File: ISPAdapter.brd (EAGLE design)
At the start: 68 x 38 mm, 4 parts

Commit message: Tweaks
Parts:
- moved JP2 0.92 mm to (33.4, 36.0)
- moved JP1 0.70 mm to (41.0, 36.0)
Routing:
- net GND: track 1.41 -> 2.40 mm
- net VCC: track 52.9 -> 52.1 mm
- net DGND: track 44.4 -> 43.6 mm
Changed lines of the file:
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@@
 <hole x="57" y="21" drill="2"/>
 <hole x="15" y="21" drill="2"/>
-<text x="41.7" y="34" size="1" layer="107" font="vector" ratio="20" rot="SR270" align="center-left">GND</text>
-<text x="44.3" y="34" size="1" layer="107" font="vector" ratio="20" rot="SR270" align="center-left">+5V</text>
+<text x="41" y="34" size="1" layer="107" font="vector" ratio="20" rot="SR270" align="center-left">GND</text>
+<text x="43.6" y="34" size="1" layer="107" font="vector" ratio="20" rot="SR270" align="center-left">+5V</text>
 <text x="26" y="11" size="1" layer="107" font="vector" ratio="20" rot="SR0">1 MISO</text>
 <text x="19" y="11" size="1" layer="107" font="vector" ratio="20" rot="SR0">2 VCC</text>
@@
 <wire x1="18" y1="10" x2="18" y2="17" width="0.2032" layer="107"/>
 <wire x1="25" y1="17" x2="25" y2="10" width="0.2032" layer="107"/>
-<text x="22.6" y="23.5" size="0.8128" layer="107" font="vector" ratio="20" align="top-center">1</text>
-<text x="21.6" y="23.5" size="0.8128" layer="107" font="vector" ratio="20" align="top-center">2</text>
-<text x="20.6" y="23.5" size="0.8128" layer="107" font="vector" ratio="20" align="top-center">3</text>
-<text x="19.6" y="23.5" size="0.8128" layer="107" font="vector" ratio="20" align="top-center">4</text>
-<text x="18.6" y="23.5" size="0.8128" layer="107" font="vector" ratio="20" align="top-center">5</text>
-<text x="17.6" y="23.5" size="0.8128" layer="107" font="vector" ratio="20" align="top-center">6</text>
+<text x="22.6" y="23.4" size="0.8128" layer="107" font="vector" ratio="20" align="top-center">1</text>
+<text x="21.6" y="23.4" size="0.8128" layer="107" font="vector" ratio="20" align="top-center">2</text>
+<text x="20.6" y="23.4" size="0.8128" layer="107" font="vector" ratio="20" align="top-center">3</text>
+<text x="19.6" y="23.4" size="0.8128" layer="107" font="vector" ratio="20" align="top-center">4</text>
+<text x="18.6" y="23.4" size="0.8128" layer="107" font="vector" ratio="20" align="top-center">5</text>
+<text x="17.6" y="23.4" size="0.8128" layer="107" font="vector" ratio="20" align="top-center">6</text>
 <circle x="27" y="30.4" radius="1.7" width="0.5" layer="107"/>
 <hole x="36" y="11.6" drill="2"/>
@@
 <circle x="36" y="6.9" radius="1.7" width="0.5" layer="107"/>
 <circle x="15" y="21" radius="1.7" width="0.5" layer="107"/>
-<text x="34.3" y="34" size="1" layer="107" font="vector" ratio="20" rot="SR270" align="center-left">GND</text>
+<text x="33.4" y="34" size="1" layer="107" font="vector" ratio="20" rot="SR270" align="center-left">GND</text>
 </plain>
 <attributes>
@@
 <param name="srMinRoundness" value="0mil"/>
 <param name="srMaxRoundness" value="0mil"/>
-<param name="slThermalIsolate" value="10mil"/>
+<param name="slThermalIsolate" value="20mil"/>
 <param name="slThermalsForVias" value="0"/>
 <param name="dpMaxLengthDifference" value="10mm"/>
@@
 <attribute name="DIGIKEY_PART_#" value="732-5394-ND" x="6" y="19" size="1.778" layer="27" display="off"/>
 </element>
-<element name="JP1" library="SparkFun-Connectors" package="1X02" value="M02PTH" x="41.7" y="36"/>
+<element name="JP1" library="SparkFun-Connectors" package="1X02" value="M02PTH" x="41" y="36"/>
 <element name="U$1" library="dubec" package="AVX9258-8P" value="AVX9258" x="19" y="27">
 <attribute name="MANUFACTURER" value="AVX Corporation" x="19" y="27" size="1.778" layer="27" display="off"/>
@@
 <attribute name="DIGIKEY_PART_#" value="478-5495-1-ND" x="19" y="27" size="1.778" layer="27" display="off"/>
 </element>
-<element name="JP2" library="SparkFun-Connectors" package="1X01" value="M01PTH" x="34.3" y="36"/>
+<element name="JP2" library="SparkFun-Connectors" package="1X01" value="M01PTH" x="33.38" y="36"/>
 </elements>
 <signals>
@@
 <contactref element="JP1" pad="2"/>
 <contactref element="U$1" pad="2"/>
-<wire x1="44.24" y1="36" x2="35.66" y2="27.42" width="0.7" layer="1"/>
-<wire x1="16.76" y1="16.7" x2="11.3" y2="16.7" width="0.7" layer="1"/>
-<wire x1="11.3" y1="16.7" x2="9.6" y2="15" width="0.7" layer="1"/>
-<wire x1="9.6" y1="15" x2="6.19" y2="15" width="0.7" layer="1"/>
-<wire x1="6.19" y1="15" x2="4.73" y2="16.46" width="0.7" layer="1"/>
+<wire x1="43.54" y1="36" x2="34.96" y2="27.42" width="0.7" layer="1"/>
+<wire x1="16.76" y1="16.7" x2="11.2" y2="16.7" width="0.3048" layer="1"/>
+<wire x1="11.2" y1="16.7" x2="9.6" y2="15.1" width="0.3048" layer="1"/>
+<wire x1="9.6" y1="15.1" x2="6.09" y2="15.1" width="0.3048" layer="1"/>
+<wire x1="6.09" y1="15.1" x2="4.73" y2="16.46" width="0.3048" layer="1"/>
 <wire x1="21.5" y1="24.15" x2="21.5" y2="24.8" width="0.7" layer="1"/>
-<wire x1="35.66" y1="27.42" x2="26.22" y2="27.42" width="0.7" layer="1"/>
-<wire x1="16.76" y1="16.7" x2="24" y2="23.94" width="0.7" layer="1"/>
+<wire x1="34.96" y1="27.42" x2="26.22" y2="27.42" width="0.7" layer="1"/>
+<wire x1="16.76" y1="16.7" x2="24" y2="23.94" width="0.3048" layer="1"/>
 <wire x1="26.22" y1="27.42" x2="24" y2="25.2" width="0.7" layer="1"/>
 <wire x1="24" y1="25.2" x2="21.9" y2="25.2" width="0.7" layer="1"/>
 <wire x1="21.9" y1="25.2" x2="21.5" y2="24.8" width="0.7" layer="1"/>
-<wire x1="24" y1="23.94" x2="24" y2="25.2" width="0.7" layer="1"/>
+<wire x1="24" y1="23.94" x2="24" y2="25.2" width="0.3048" layer="1"/>
 </signal>
 <signal name="MOSI">
@@
 <contactref element="JP1" pad="1"/>
 <contactref element="U$1" pad="6"/>
-<wire x1="35.3" y1="28.5" x2="23.1" y2="28.5" width="0.7" layer="1"/>
+<wire x1="34.5" y1="28.5" x2="23.1" y2="28.5" width="0.7" layer="1"/>
 <wire x1="23.1" y1="28.5" x2="19.8" y2="25.2" width="0.7" layer="1"/>
 <wire x1="19.8" y1="25.2" x2="17.9" y2="25.2" width="0.7" layer="1"/>
 <wire x1="17.9" y1="25.2" x2="17.5" y2="24.8" width="0.7" layer="1"/>
 <wire x1="17.5" y1="24.8" x2="17.5" y2="24.15" width="0.7" layer="1"/>
-<wire x1="4.73" y1="21.54" x2="6.19" y2="23" width="0.7" layer="1"/>
-<wire x1="6.19" y1="23" x2="17" y2="23" width="0.7" layer="1"/>
-<wire x1="17" y1="23" x2="17.5" y2="23.5" width="0.7" layer="1"/>
-<wire x1="17.5" y1="23.5" x2="17.5" y2="24.15" width="0.7" layer="1"/>
-<wire x1="35.3" y1="28.5" x2="41.7" y2="34.9" width="0.7" layer="1"/>
-<wire x1="41.7" y1="34.9" x2="41.7" y2="36" width="0.7" layer="1"/>
+<wire x1="4.73" y1="21.54" x2="6.09" y2="22.9" width="0.3048" layer="1"/>
+<wire x1="6.09" y1="22.9" x2="16.9" y2="22.9" width="0.3048" layer="1"/>
+<wire x1="16.9" y1="22.9" x2="17.5" y2="23.5" width="0.3048" layer="1"/>
+<wire x1="17.5" y1="23.5" x2="17.5" y2="24.15" width="0.3048" layer="1"/>
+<wire x1="34.5" y1="28.5" x2="41" y2="35" width="0.7" layer="1"/>
+<wire x1="41" y1="35" x2="41" y2="36" width="0.7" layer="1"/>
 </signal>
 <signal name="MISO">
@@
 </signal>
 <signal name="GND">
-<polygon width="0.3556" layer="1">
+<polygon width="0.3556" layer="1" isolate="0.508">
 <vertex x="0" y="0"/>
 <vertex x="0" y="38"/>
@@
 <via x="63" y="5" extent="1-16" drill="3.1"/>
 <contactref element="JP2" pad="1"/>
-<wire x1="40.7" y1="37" x2="41.7" y2="36" width="0.3048" layer="1"/>
-<polygon width="0.2032" layer="16">
+<wire x1="39.3" y1="36" x2="41.7" y2="36" width="0.3048" layer="1"/>
+<polygon width="0.254" layer="16" isolate="0.508">
 <vertex x="0" y="0"/>
 <vertex x="0" y="38"/>

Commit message: Emblem to library; tweaks
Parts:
- added U$2: (no value), dubec:TF-EMBLEM
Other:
- board text added: "201x-xx-xx"
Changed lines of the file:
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@@
 <?xml version="1.0" encoding="utf-8"?>
 <!DOCTYPE eagle SYSTEM "eagle.dtd">
-<eagle version="7.4.0">
+<eagle version="7.5.0">
 <drawing>
 <settings>
@@
 for Super DUBEC.
 Rev. 1</text>
-<text x="4" y="3.5" size="1" layer="107" font="vector" ratio="20" align="top-left">http://TURBOFUNCTION.com/fpv</text>
+<text x="5.5" y="4" size="1" layer="107" font="vector" ratio="20" align="center-left">http://TURBOFUNCTION.com/fpv</text>
 <text x="18" y="18" size="1" layer="107" font="vector" ratio="20">ISP connector pins:</text>
 <hole x="36" y="6.9" drill="2"/>
@@
 <circle x="15" y="21" radius="1.7" width="0.5" layer="107"/>
 <text x="33.4" y="34" size="1" layer="107" font="vector" ratio="20" rot="SR270" align="center-left">GND</text>
+<text x="5.5" y="2.4" size="0.8128" layer="107" font="vector" ratio="20" align="center-left">201x-xx-xx</text>
 </plain>
 <attributes>
@@
 </element>
 <element name="JP2" library="SparkFun-Connectors" package="1X01" value="M01PTH" x="33.38" y="36"/>
+<element name="U$2" library="dubec" package="TF-EMBLEM" value="" x="3.1" y="3.3"/>
 </elements>
 <signals>

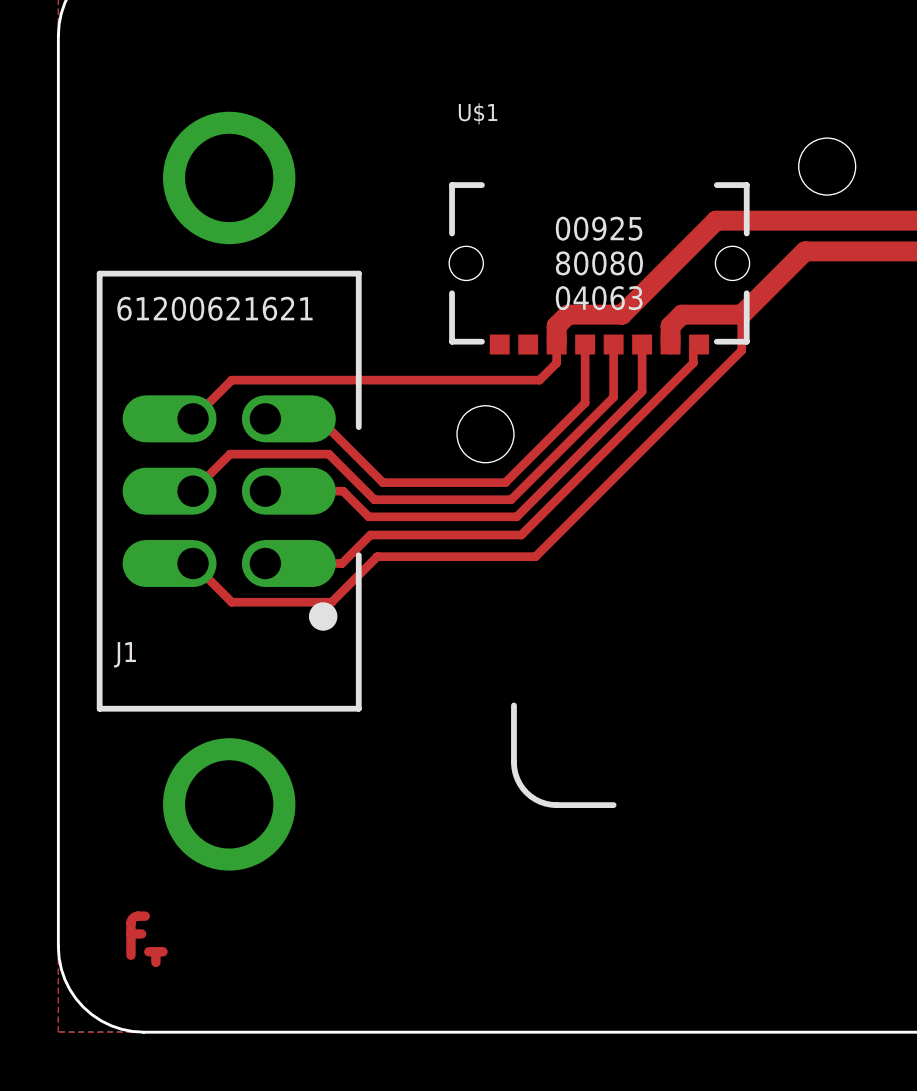
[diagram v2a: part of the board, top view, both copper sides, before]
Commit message: Separate connector mounting pad
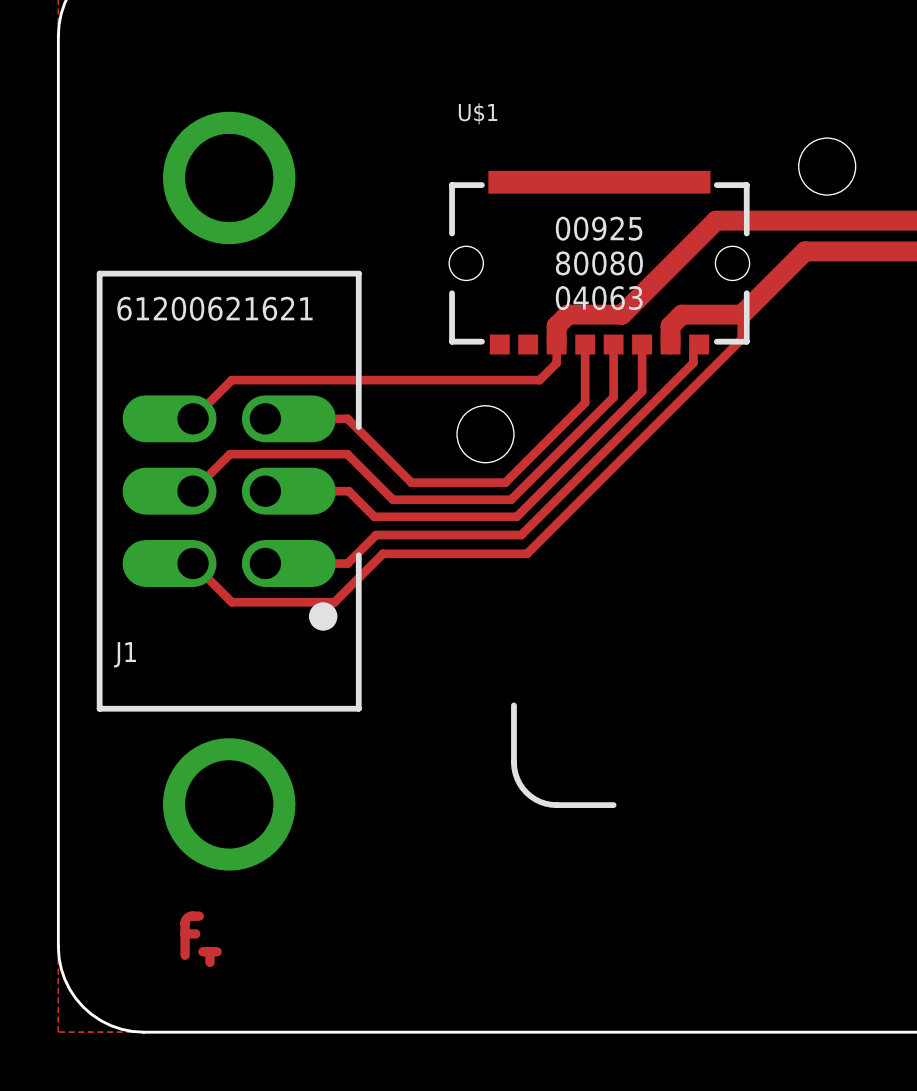
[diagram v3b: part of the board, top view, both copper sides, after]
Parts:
- moved U$2 1.90 mm to (5.00, 3.30)
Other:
- board text added: "AVR ISP adapter board for Super DUBEC. Rev. 2"
- board text removed: "AVR ISP adapter board for Super DUBEC. Rev. 1"
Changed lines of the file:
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@@
 <layer number="14" name="Route14" color="1" fill="6" visible="no" active="no"/>
 <layer number="15" name="Route15" color="4" fill="6" visible="no" active="no"/>
-<layer number="16" name="Bottom" color="1" fill="1" visible="no" active="yes"/>
+<layer number="16" name="Bottom" color="1" fill="1" visible="yes" active="yes"/>
 <layer number="17" name="Pads" color="2" fill="1" visible="yes" active="yes"/>
 <layer number="18" name="Vias" color="2" fill="1" visible="yes" active="yes"/>
@@
 <layer number="20" name="Dimension" color="15" fill="1" visible="yes" active="yes"/>
 <layer number="21" name="tPlace" color="7" fill="1" visible="yes" active="yes"/>
-<layer number="22" name="bPlace" color="7" fill="1" visible="no" active="yes"/>
+<layer number="22" name="bPlace" color="7" fill="1" visible="yes" active="yes"/>
 <layer number="23" name="tOrigins" color="15" fill="1" visible="yes" active="yes"/>
-<layer number="24" name="bOrigins" color="15" fill="1" visible="no" active="yes"/>
+<layer number="24" name="bOrigins" color="15" fill="1" visible="yes" active="yes"/>
 <layer number="25" name="tNames" color="7" fill="1" visible="no" active="yes"/>
 <layer number="26" name="bNames" color="7" fill="1" visible="no" active="yes"/>
@@
 <layer number="28" name="bValues" color="7" fill="1" visible="no" active="yes"/>
 <layer number="29" name="tStop" color="7" fill="3" visible="yes" active="yes"/>
-<layer number="30" name="bStop" color="7" fill="6" visible="no" active="yes"/>
-<layer number="31" name="tCream" color="7" fill="4" visible="no" active="yes"/>
-<layer number="32" name="bCream" color="7" fill="5" visible="no" active="yes"/>
+<layer number="30" name="bStop" color="7" fill="6" visible="yes" active="yes"/>
+<layer number="31" name="tCream" color="7" fill="4" visible="yes" active="yes"/>
+<layer number="32" name="bCream" color="7" fill="5" visible="yes" active="yes"/>
 <layer number="33" name="tFinish" color="6" fill="3" visible="yes" active="yes"/>
-<layer number="34" name="bFinish" color="6" fill="6" visible="no" active="yes"/>
+<layer number="34" name="bFinish" color="6" fill="6" visible="yes" active="yes"/>
 <layer number="35" name="tGlue" color="7" fill="4" visible="yes" active="yes"/>
-<layer number="36" name="bGlue" color="7" fill="5" visible="no" active="yes"/>
+<layer number="36" name="bGlue" color="7" fill="5" visible="yes" active="yes"/>
 <layer number="37" name="tTest" color="7" fill="1" visible="yes" active="yes"/>
-<layer number="38" name="bTest" color="7" fill="1" visible="no" active="yes"/>
+<layer number="38" name="bTest" color="7" fill="1" visible="yes" active="yes"/>
 <layer number="39" name="tKeepout" color="4" fill="11" visible="yes" active="yes"/>
-<layer number="40" name="bKeepout" color="1" fill="11" visible="no" active="yes"/>
+<layer number="40" name="bKeepout" color="1" fill="11" visible="yes" active="yes"/>
 <layer number="41" name="tRestrict" color="4" fill="10" visible="yes" active="yes"/>
-<layer number="42" name="bRestrict" color="1" fill="10" visible="no" active="yes"/>
+<layer number="42" name="bRestrict" color="1" fill="10" visible="yes" active="yes"/>
 <layer number="43" name="vRestrict" color="2" fill="10" visible="no" active="yes"/>
 <layer number="44" name="Drills" color="7" fill="1" visible="no" active="yes"/>
-<layer number="45" name="Holes" color="7" fill="1" visible="yes" active="yes"/>
+<layer number="45" name="Holes" color="7" fill="1" visible="no" active="yes"/>
 <layer number="46" name="Milling" color="3" fill="1" visible="no" active="yes"/>
 <layer number="47" name="Measures" color="7" fill="1" visible="yes" active="yes"/>
@@
 <layer number="49" name="Reference" color="7" fill="1" visible="no" active="yes"/>
 <layer number="50" name="dxf" color="7" fill="1" visible="no" active="no"/>
-<layer number="51" name="tDocu" color="7" fill="1" visible="yes" active="yes"/>
+<layer number="51" name="tDocu" color="7" fill="1" visible="no" active="yes"/>
 <layer number="52" name="bDocu" color="7" fill="1" visible="no" active="yes"/>
 <layer number="53" name="tGND_GNDA" color="7" fill="9" visible="no" active="no"/>
@@
 <circle x="27" y="30.4" radius="1.7" width="0.5" layer="107"/>
 <hole x="36" y="11.6" drill="2"/>
-<text x="10" y="36" size="1" layer="107" font="vector" ratio="20" align="top-left">AVR ISP adapter board
+<text x="30" y="27" size="1.3" layer="107" font="vector" ratio="20" align="top-left">AVR ISP adapter board
 for Super DUBEC.
-Rev. 1</text>
-<text x="5.5" y="4" size="1" layer="107" font="vector" ratio="20" align="center-left">http://TURBOFUNCTION.com/fpv</text>
+Rev. 2</text>
+<text x="7.5" y="3.1" size="1.1" layer="107" font="vector" ratio="20">http://TURBOFUNCTION.com/fpv</text>
 <text x="18" y="18" size="1" layer="107" font="vector" ratio="20">ISP connector pins:</text>
 <hole x="36" y="6.9" drill="2"/>
@@
 <circle x="15" y="21" radius="1.7" width="0.5" layer="107"/>
 <text x="33.4" y="34" size="1" layer="107" font="vector" ratio="20" rot="SR270" align="center-left">GND</text>
-<text x="5.5" y="2.4" size="0.8128" layer="107" font="vector" ratio="20" align="center-left">201x-xx-xx</text>
+<text x="7.5" y="1.6" size="0.8128" layer="107" font="vector" ratio="20">201x-xx-xx</text>
+<rectangle x1="15.1" y1="29.45" x2="22.9" y2="30.25" layer="1"/>
 </plain>
 <attributes>
@@
 </element>
 <element name="JP2" library="SparkFun-Connectors" package="1X01" value="M01PTH" x="33.38" y="36"/>
-<element name="U$2" library="dubec" package="TF-EMBLEM" value="" x="3.1" y="3.3"/>
+<element name="U$2" library="dubec" package="TF-EMBLEM" value="" x="5" y="3.3"/>
 </elements>
 <signals>
@@
 <contactref element="U$1" pad="2"/>
 <wire x1="43.54" y1="36" x2="34.96" y2="27.42" width="0.7" layer="1"/>
-<wire x1="16.76" y1="16.7" x2="11.2" y2="16.7" width="0.3048" layer="1"/>
-<wire x1="11.2" y1="16.7" x2="9.6" y2="15.1" width="0.3048" layer="1"/>
-<wire x1="9.6" y1="15.1" x2="6.09" y2="15.1" width="0.3048" layer="1"/>
+<wire x1="16.46" y1="16.8" x2="11.4" y2="16.8" width="0.3048" layer="1"/>
+<wire x1="11.4" y1="16.8" x2="9.7" y2="15.1" width="0.3048" layer="1"/>
+<wire x1="9.7" y1="15.1" x2="6.09" y2="15.1" width="0.3048" layer="1"/>
 <wire x1="6.09" y1="15.1" x2="4.73" y2="16.46" width="0.3048" layer="1"/>
 <wire x1="21.5" y1="24.15" x2="21.5" y2="24.8" width="0.7" layer="1"/>
 <wire x1="34.96" y1="27.42" x2="26.22" y2="27.42" width="0.7" layer="1"/>
-<wire x1="16.76" y1="16.7" x2="24" y2="23.94" width="0.3048" layer="1"/>
+<wire x1="16.46" y1="16.8" x2="24" y2="24.34" width="0.3048" layer="1"/>
 <wire x1="26.22" y1="27.42" x2="24" y2="25.2" width="0.7" layer="1"/>
 <wire x1="24" y1="25.2" x2="21.9" y2="25.2" width="0.7" layer="1"/>
 <wire x1="21.9" y1="25.2" x2="21.5" y2="24.8" width="0.7" layer="1"/>
-<wire x1="24" y1="23.94" x2="24" y2="25.2" width="0.3048" layer="1"/>
+<wire x1="24" y1="24.34" x2="24" y2="25.2" width="0.3048" layer="1"/>
 </signal>
 <signal name="MOSI">
@@
 <wire x1="19.5" y1="24.15" x2="19.5" y2="22.3" width="0.3048" layer="1"/>
 <wire x1="19.5" y1="22.3" x2="15.9" y2="18.7" width="0.3048" layer="1"/>
-<wire x1="15.9" y1="18.7" x2="11.1" y2="18.7" width="0.3048" layer="1"/>
-<wire x1="11.1" y1="18.7" x2="9.5" y2="20.3" width="0.3048" layer="1"/>
-<wire x1="9.5" y1="20.3" x2="6.03" y2="20.3" width="0.3048" layer="1"/>
+<wire x1="15.9" y1="18.7" x2="11.75" y2="18.7" width="0.3048" layer="1"/>
+<wire x1="11.75" y1="18.7" x2="10.15" y2="20.3" width="0.3048" layer="1"/>
+<wire x1="10.15" y1="20.3" x2="6.03" y2="20.3" width="0.3048" layer="1"/>
 <wire x1="6.03" y1="20.3" x2="4.73" y2="19" width="0.3048" layer="1"/>
 </signal>
@@
 <contactref element="U$1" pad="1"/>
 <wire x1="22.3" y1="23.5" x2="16.26" y2="17.46" width="0.3048" layer="1"/>
-<wire x1="16.26" y1="17.46" x2="10.96" y2="17.46" width="0.3048" layer="1"/>
-<wire x1="10.96" y1="17.46" x2="9.96" y2="16.46" width="0.3048" layer="1"/>
-<wire x1="9.96" y1="16.46" x2="7.27" y2="16.46" width="0.3048" layer="1"/>
+<wire x1="16.26" y1="17.46" x2="11.16" y2="17.46" width="0.3048" layer="1"/>
+<wire x1="11.16" y1="17.46" x2="10.16" y2="16.46" width="0.3048" layer="1"/>
+<wire x1="10.16" y1="16.46" x2="7.27" y2="16.46" width="0.3048" layer="1"/>
 <wire x1="22.3" y1="23.5" x2="22.3" y2="23.95" width="0.3048" layer="1"/>
 <wire x1="22.3" y1="23.95" x2="22.5" y2="24.15" width="0.3048" layer="1"/>
@@
 <wire x1="20.5" y1="24.15" x2="20.5" y2="22.5" width="0.3048" layer="1"/>
 <wire x1="20.5" y1="22.5" x2="16.1" y2="18.1" width="0.3048" layer="1"/>
-<wire x1="16.1" y1="18.1" x2="10.9" y2="18.1" width="0.3048" layer="1"/>
-<wire x1="10.9" y1="18.1" x2="10" y2="19" width="0.3048" layer="1"/>
-<wire x1="10" y1="19" x2="7.27" y2="19" width="0.3048" layer="1"/>
+<wire x1="16.1" y1="18.1" x2="11.1" y2="18.1" width="0.3048" layer="1"/>
+<wire x1="11.1" y1="18.1" x2="10.2" y2="19" width="0.3048" layer="1"/>
+<wire x1="10.2" y1="19" x2="7.27" y2="19" width="0.3048" layer="1"/>
 </signal>
 <signal name="RESET">
@@
 <wire x1="18.5" y1="24.15" x2="18.5" y2="22.1" width="0.3048" layer="1"/>
 <wire x1="18.5" y1="22.1" x2="15.7" y2="19.3" width="0.3048" layer="1"/>
-<wire x1="15.7" y1="19.3" x2="11.4" y2="19.3" width="0.3048" layer="1"/>
-<wire x1="11.4" y1="19.3" x2="9.16" y2="21.54" width="0.3048" layer="1"/>
-<wire x1="9.16" y1="21.54" x2="7.27" y2="21.54" width="0.3048" layer="1"/>
+<wire x1="15.7" y1="19.3" x2="12.4" y2="19.3" width="0.3048" layer="1"/>
+<wire x1="12.4" y1="19.3" x2="10.16" y2="21.54" width="0.3048" layer="1"/>
+<wire x1="10.16" y1="21.54" x2="7.27" y2="21.54" width="0.3048" layer="1"/>
 </signal>
 <signal name="GND">
